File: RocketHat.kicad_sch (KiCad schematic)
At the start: 24 parts, among them J1 Screw_Terminal_01x02, J10 Raspberry_Pi_2_3, J2 Conn_01x06_Female, J3 Conn_01x06_Female, J4 Conn_01x07_Female, J5 Conn_01x06_Female, J6 Conn_01x04_Female, J7 Conn_01x10_Female, J8 Conn_01x02, J9 Conn_01x10_Female, Q1 FQP27P06, SW1 SW_Reed_SPDT, U1 CAT24C128

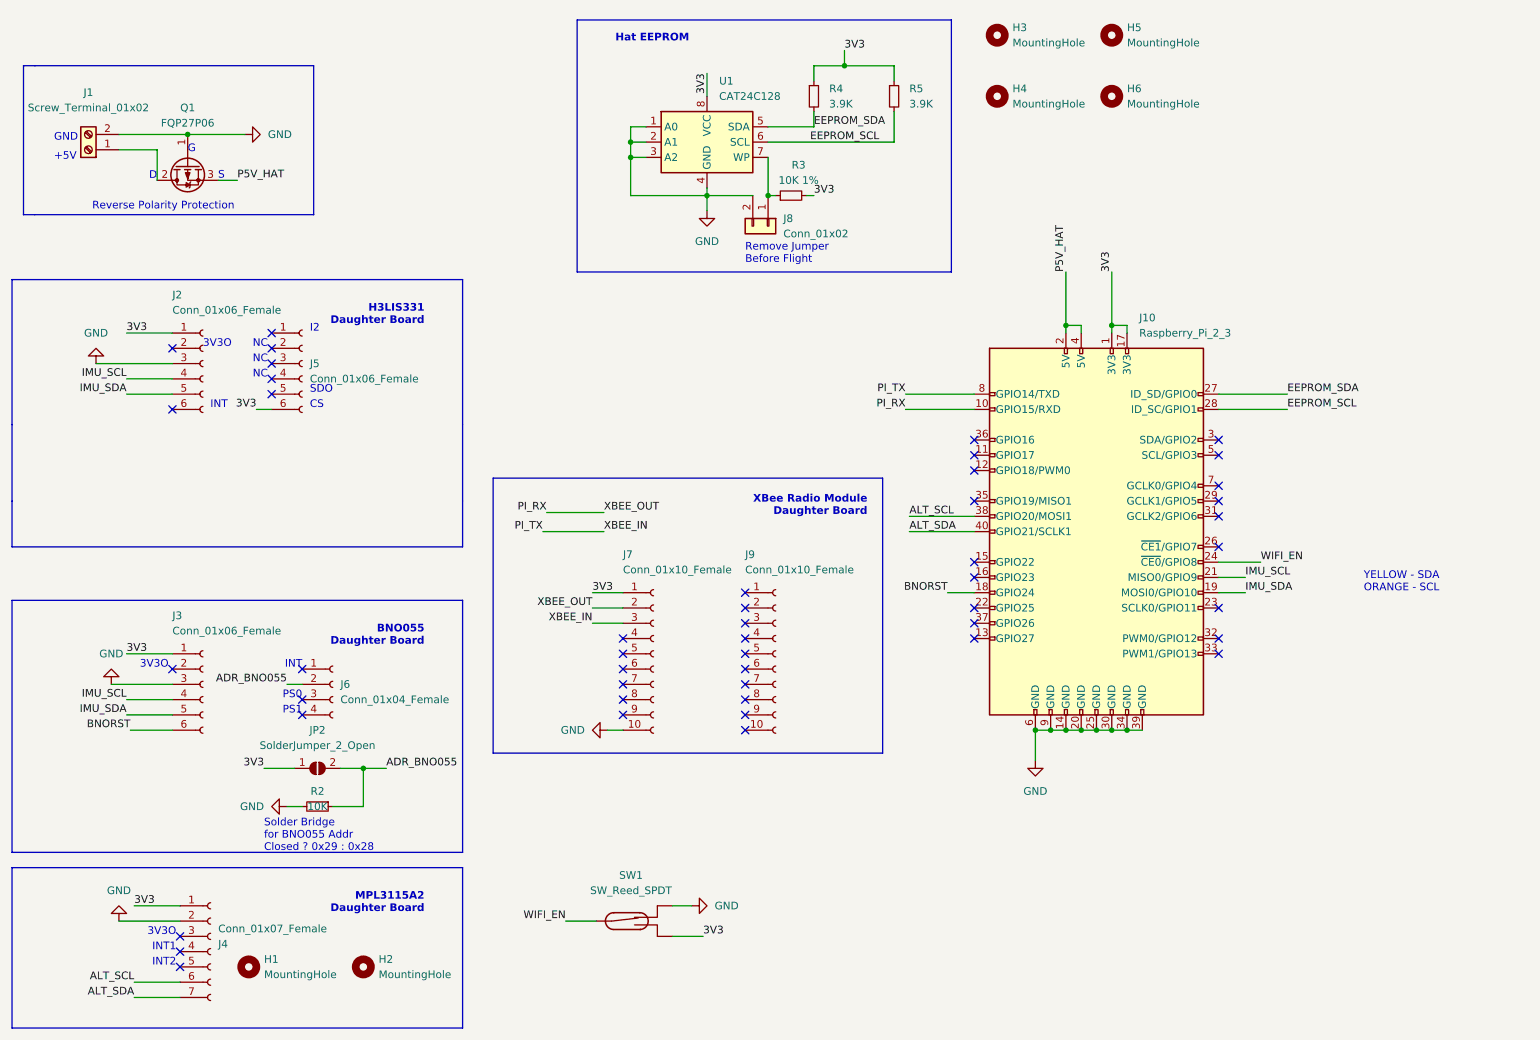
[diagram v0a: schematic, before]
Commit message: Added Buzzer
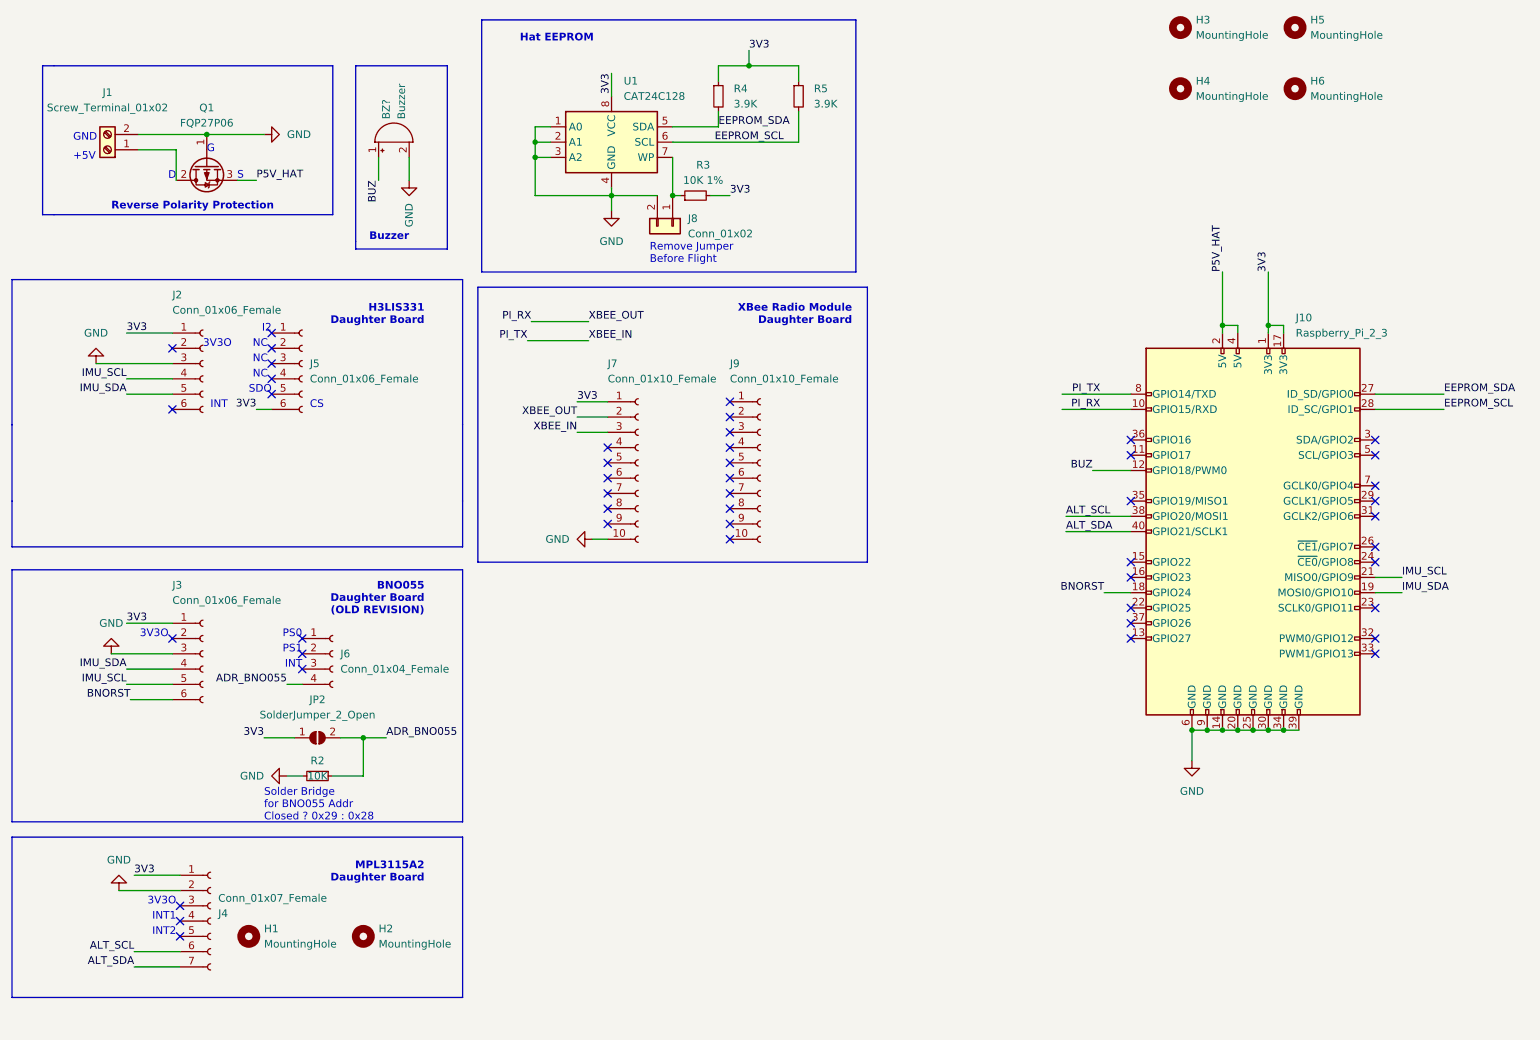
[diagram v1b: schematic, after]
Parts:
- removed SW1: SW_Reed_SPDT, Button_Switch_THT:KSA_Tactile_SPST, symbol Switch:SW_Reed_SPDT
- added BZ?: Buzzer, symbol Device:Buzzer
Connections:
- net ADR_BNO055: now also J6.4 (Pin_4); no longer J6.2 (Pin_2)
- net GND: now also BZ?.2 (+)
- net IMU_SCL: now also J3.5 (Pin_5); no longer J3.4 (Pin_4)
- net IMU_SDA: now also J3.4 (Pin_4); no longer J3.5 (Pin_5)
- net BUZ: now reaches J10.12 (GPIO18/PWM0)
- net BUZ: now also BZ?.1 (-)
- net WIFI_EN: no longer names the net of J10.24 (~{CE0}/GPIO8)
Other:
- note added: "BNO055 Daughter Board (OLD REVISION)"
- note added: "Buzzer"
- note removed: "BNO055 Daughter Board"
- note removed: "YELLOW - SDA ORANGE - SCL"
- company: Rose-Hulman Rocketry Team -> (none)
- title: Rocket IMU / Radio Sensor Hat -> (none)
- moved on the sheet: H1, H2, H3, H4, H5, H6, J1, J10, J3, J4, J6, J7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

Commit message: Updated EEPROM WP
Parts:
- removed J8: Conn_01x02, Connector_PinHeader_2.54mm:PinHeader_1x02_P2.54mm_Vertical, symbol Connector_Generic:Conn_01x02
- removed R3: 10K 1%, Resistor_THT:R_Axial_DIN0204_L3.6mm_D1.6mm_P5.08mm_Horizontal, symbol Device:R_Small
- added JP1: SolderJumper_2_Bridged, symbol Jumper:SolderJumper_2_Bridged
- added R1: 10k, symbol Device:R_Small
- gave numbers to parts that had none: 1
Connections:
- net 3V3: now also JP1.1 (A)
- net GND: now also R1.1
- net at U1.7 (WP): now also JP1.2 (B), R1.2
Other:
- note added: "XBEE_IN"
- note added: "XBEE_OUT"

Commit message: Updated Schematics and Footprints
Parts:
- BZ1: footprint (none) -> Buzzer_Beeper:Buzzer_12x9.5RM7.6
- JP1: footprint (none) -> Jumper:SolderJumper-2_P1.3mm_Bridged_RoundedPad1.0x1.5mm
- R1: footprint (none) -> Resistor_THT:R_Axial_DIN0204_L3.6mm_D1.6mm_P5.08mm_Horizontal
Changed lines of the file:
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@@
       (effects (font (size 1.27 1.27)) (justify right))
     )
-    (property "Footprint" "" (id 2) (at 144.145 45.085 0)
+    (property "Footprint" "Resistor_THT:R_Axial_DIN0204_L3.6mm_D1.6mm_P5.08mm_Horizontal" (id 2) (at 144.145 45.085 0)
       (effects (font (size 1.27 1.27)) hide)
     )
@@
       (effects (font (size 1.27 1.27)) (justify right))
     )
-    (property "Footprint" "" (id 2) (at 155.575 45.72 0)
+    (property "Footprint" "Jumper:SolderJumper-2_P1.3mm_Bridged_RoundedPad1.0x1.5mm" (id 2) (at 155.575 45.72 0)
       (effects (font (size 1.27 1.27)) hide)
     )
@@
       (effects (font (size 1.27 1.27)) (justify left))
     )
-    (property "Footprint" "" (id 2) (at 93.98 40.005 90)
+    (property "Footprint" "Buzzer_Beeper:Buzzer_12x9.5RM7.6" (id 2) (at 93.98 40.005 90)
       (effects (font (size 1.27 1.27)) hide)
     )
@@
     )
     (path "/c57f216c-7b95-490c-b05d-64f57cf2aecb"
-      (reference "BZ1") (unit 1) (value "Buzzer") (footprint "")
+      (reference "BZ1") (unit 1) (value "Buzzer") (footprint "Buzzer_Beeper:Buzzer_12x9.5RM7.6")
     )
     (path "/9745344d-f5a4-4b56-b292-fac7f1ad12d0"
@@
     )
     (path "/aea75ec5-5279-4d47-ab09-573ae0a4819b"
-      (reference "JP1") (unit 1) (value "SolderJumper_2_Bridged") (footprint "")
+      (reference "JP1") (unit 1) (value "SolderJumper_2_Bridged") (footprint "Jumper:SolderJumper-2_P1.3mm_Bridged_RoundedPad1.0x1.5mm")
     )
     (path "/12b843c4-0c50-4529-b30c-b86b981e29d2"
@@
     )
     (path "/34cb238f-e443-47f6-b9b2-74106430007a"
-      (reference "R1") (unit 1) (value "10k") (footprint "")
+      (reference "R1") (unit 1) (value "10k") (footprint "Resistor_THT:R_Axial_DIN0204_L3.6mm_D1.6mm_P5.08mm_Horizontal")
     )
     (path "/371e2c35-1dd3-4ab9-a165-5756dbc0abde"
